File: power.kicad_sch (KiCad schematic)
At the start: 9 parts

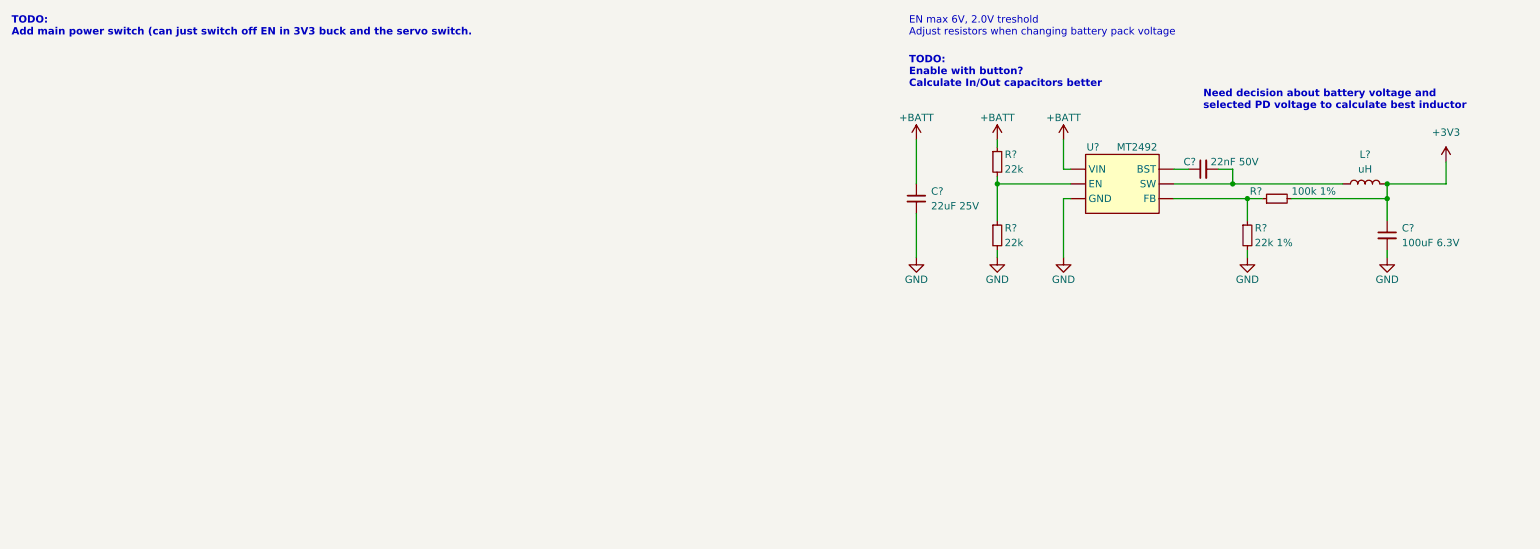
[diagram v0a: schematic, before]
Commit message: Added PD chip with footprint, I2C extension connectors
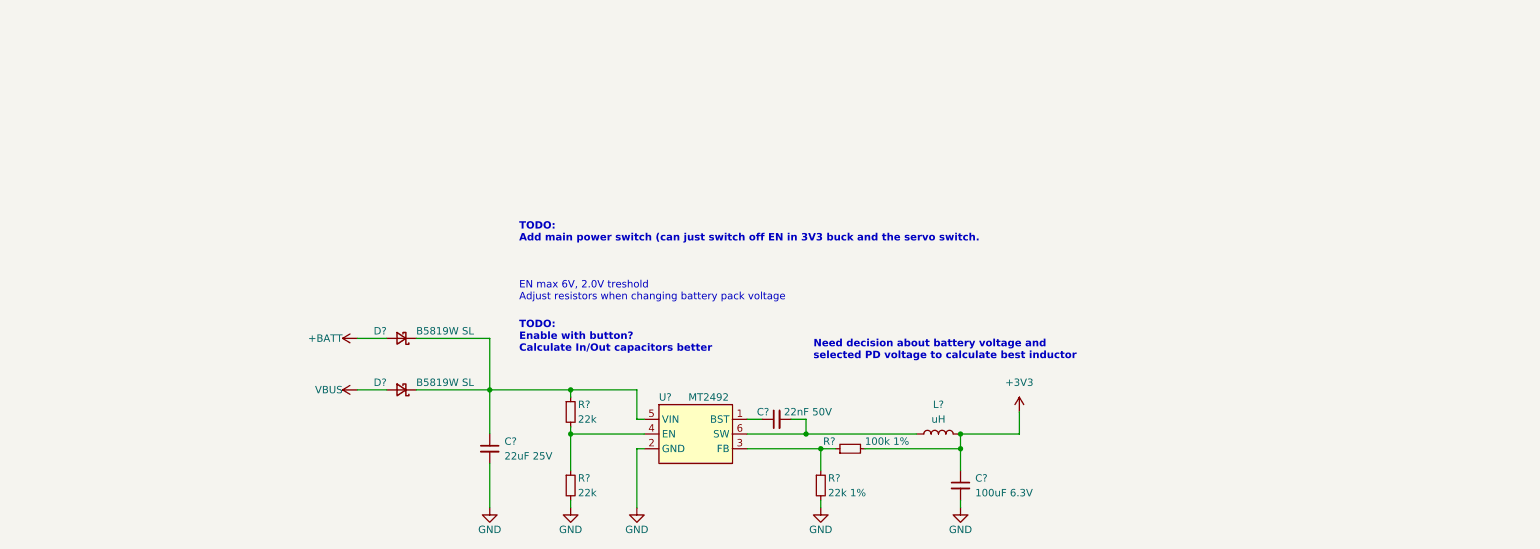
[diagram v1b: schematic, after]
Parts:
- added D? (x2): B5819W SL, Diode_SMD:D_SOD-123, symbol Device:D_Schottky_Small
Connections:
- net +BATT: now also D?.2 (A); no longer C?.1, R?.1, U?. (VIN)
- net GND: now also U?.2 (GND); no longer U?. (VIN)
- net at R?.1, R?.2: now also U?.4 (EN); no longer U?. (VIN)
- net at C?.2, L?.1: now also U?.6 (SW); no longer U?. (VIN)
- net at C?.1: now also U?.1 (BST); no longer U?. (VIN)
- net at R?.1, R?.1: now also U?.3 (FB); no longer U?. (VIN)
- new net: C?.1, D?.1 (K), D?.1 (K), R?.1, U?.5 (VIN)
- new net VBUS: D?.2 (A)
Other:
- moved on the sheet: C?, L?, R?
